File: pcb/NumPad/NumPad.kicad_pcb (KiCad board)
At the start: 2 copper layers, 100 x 100 mm, 120 parts, among them IC1 IS31FL3731, J1 USB_OTG, J2 ISP, J3 GS2, J4 GS2, J5 GS2, J6 GS2, J7 Conn_01x06, SW1 +, SW10 ,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

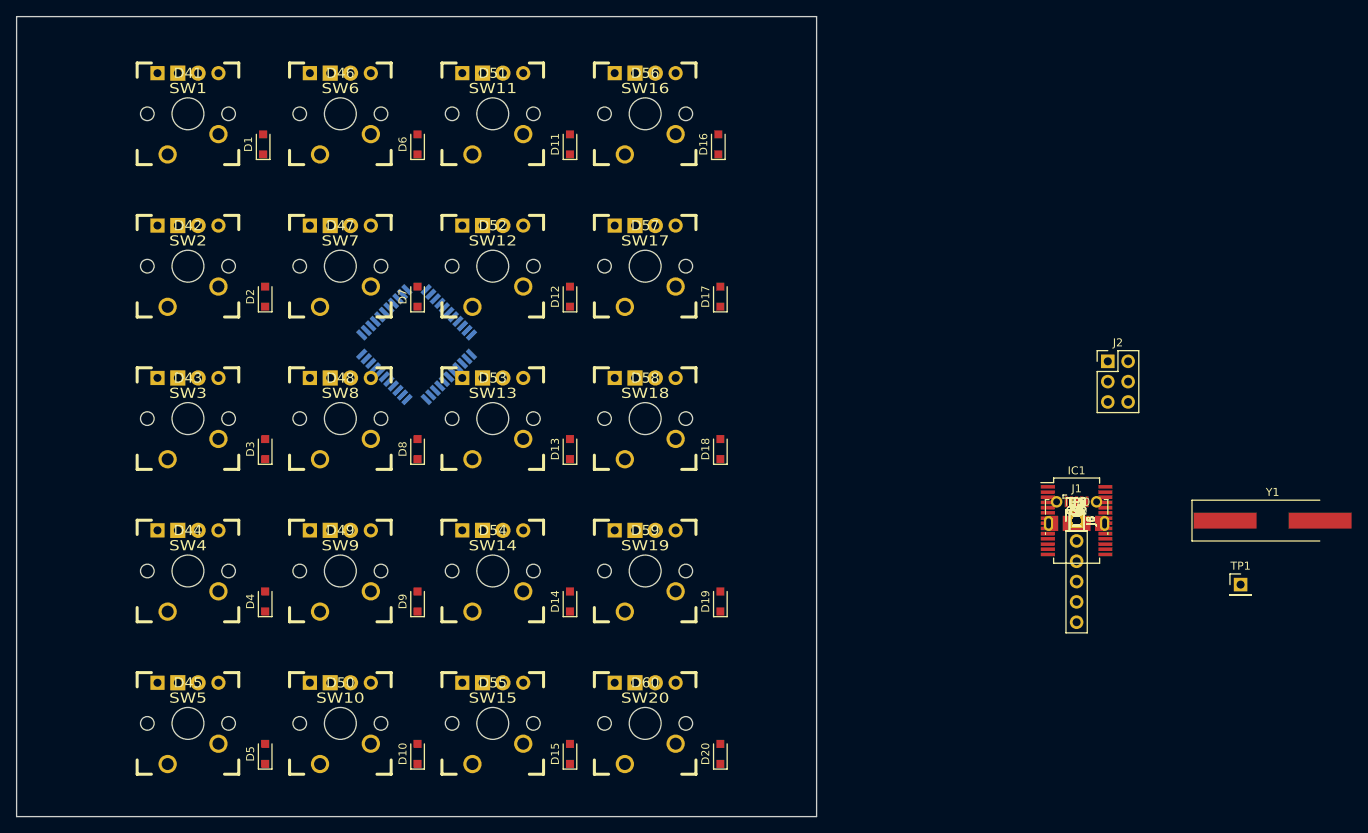
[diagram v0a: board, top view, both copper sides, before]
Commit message: changes in Numpad
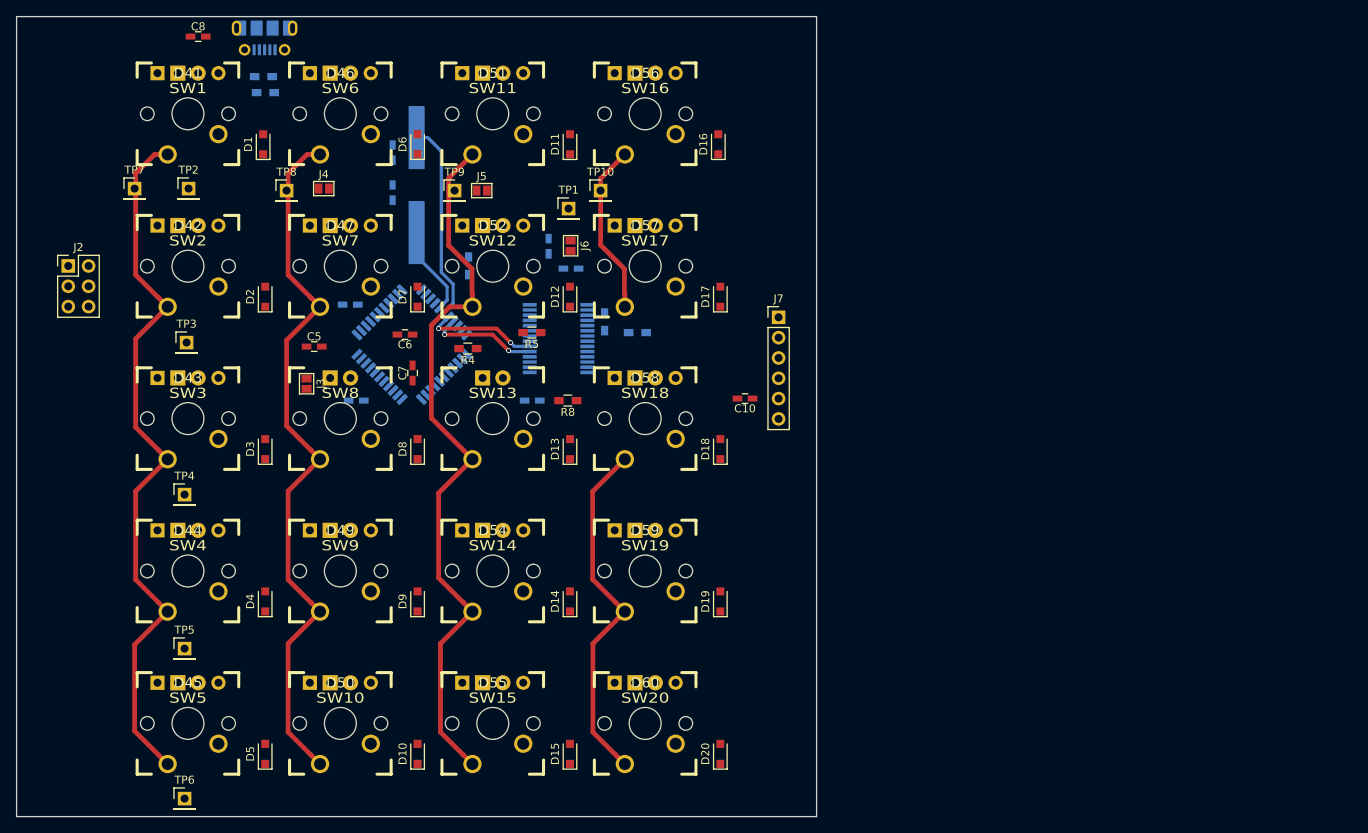
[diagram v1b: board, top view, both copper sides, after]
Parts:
- removed D48, D53: D, footprints:CHERRY_MX_DIODE
- C1, C11, C12, C2, C3, C4, C9, IC1, J1, R1, R2, R3, R6, R7, Y1: moved to B.Cu
- moved J2 130.5 mm to (47.5, 72.2)
- moved C8 125.4 mm to (63.7, 43.5)
- moved TP7 124.9 mm to (55.8, 62.5)
- moved J1 118.5 mm to (72.0, 42.8)
- moved TP2 118.5 mm to (62.5, 62.5)
- moved TP6 116.8 mm to (62.0, 138.8)
- moved R1 115.8 mm to (71.8, 48.5)
- moved Y1 114.9 mm to (91.0, 62.1), turned to 270 degrees
- moved R2 114.7 mm to (72.1, 50.5)
- moved TP3 113.5 mm to (62.2, 81.8)
- moved TP5 112.6 mm to (62.0, 120.0)
- moved TP4 111.5 mm to (62.0, 100.8)
- moved TP8 107.0 mm to (74.8, 62.8)
- moved J4 102.9 mm to (79.4, 62.5), turned to 90 degrees
- moved J3 97.8 mm to (77.2, 86.9)
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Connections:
- TP1 pad 1: Net-(TP1-Pad1) -> /Controller/SHUTDOWN
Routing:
- net /Controller/COL2: track 0.00 -> 91.4 mm
- net /Controller/COL1: track 0.00 -> 90.5 mm
- net /Controller/COL0: track 0.00 -> 90.5 mm
- net /Controller/COL3: track 0.00 -> 66.3 mm
- net Net-(C3-Pad1): track 0.00 -> 25.0 mm
- net /Controller/SCL: track 0.00 -> 14.3 mm, vias 0 -> 2
- net /Controller/SDA: track 0.00 -> 13.6 mm, vias 0 -> 2
- net Net-(C4-Pad1): track 0.00 -> 11.4 mm
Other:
- net class Default: clearance 0.2 -> 0.3
- rule trace_clearance: 0.2 -> 0.3

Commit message: changes in NumPad layout
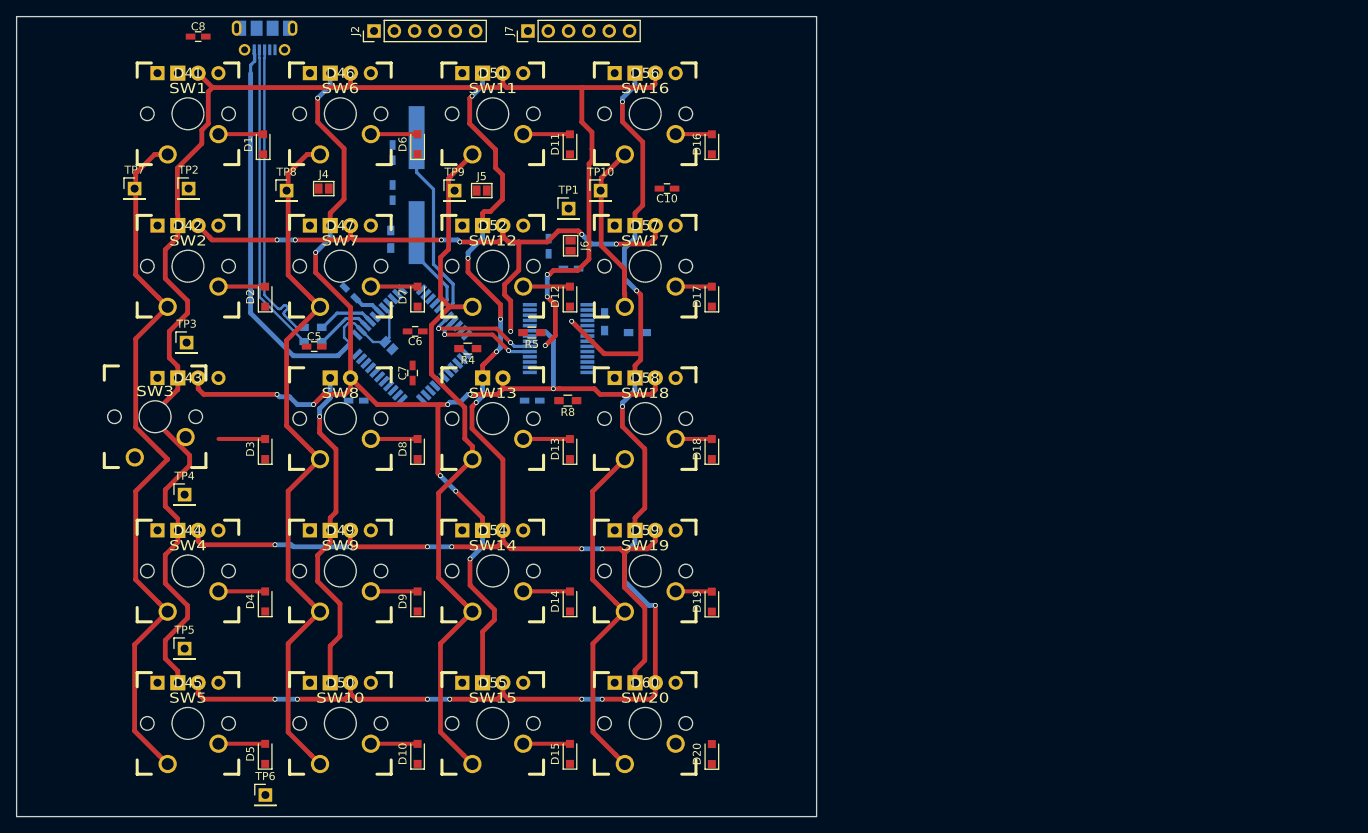
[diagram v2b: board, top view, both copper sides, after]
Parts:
- J2: footprint Pin_Headers:Pin_Header_Straight_2x03_Pitch2.54mm -> Pin_Headers:Pin_Header_Straight_1x06_Pitch2.54mm
- J3: moved to B.Cu
- moved J2 48.2 mm to (85.7, 42.8), turned to 90 degrees
- moved J7 47.6 mm to (104.9, 42.8), turned to 90 degrees
- moved R1 31.9 mm to (78.0, 79.8), turned to 180 degrees
- moved R2 31.7 mm to (78.0, 81.6), turned to 180 degrees
- moved C10 28.0 mm to (122.3, 62.5)
- moved J3 11.3 mm to (87.5, 82.1), turned to 45 degrees
- moved R3 10.3 mm to (87.8, 68.8), turned to 90 degrees
- moved TP6 10.1 mm to (72.1, 138.3)
- moved SW3 4.11 mm to (58.3, 91.0)
- moved C2 1.48 mm to (82.7, 75.5), turned to 315 degrees
- moved C6 1.34 mm to (90.8, 80.3)
- moved D19 1.06 mm to (127.9, 114.1)
- moved D20 1.06 mm to (127.9, 133.2)
- moved D17 1.06 mm to (127.9, 76.0)
- moved D18 1.06 mm to (127.9, 95.1)
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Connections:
- net Net-(J1-Pad2) renamed /Controller/USB_D-
- net Net-(J1-Pad3) renamed /Controller/USB_D+
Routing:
- net /Controller/CA1: track 0.00 -> 187.9 mm, vias 0 -> 3
- net /Controller/CA5: track 0.00 -> 159.6 mm, vias 0 -> 11
- net /Controller/CA3: track 0.00 -> 157.7 mm, vias 0 -> 10
- net /Controller/CA4: track 0.00 -> 149.4 mm, vias 0 -> 11
- net /Controller/CA2: track 0.00 -> 120.6 mm, vias 0 -> 8
- net UVCC: track 0.00 -> 61.9 mm
- net /Controller/USB_D-: track 0.00 -> 38.8 mm
- net /Controller/USB_D+: track 0.00 -> 38.8 mm
- net /Controller/D-: track 0.00 -> 7.41 mm
- net /Controller/D+: track 0.00 -> 7.28 mm
- net Net-(D7-Pad2): track 0.00 -> 5.85 mm
- net Net-(D5-Pad2): track 0.00 -> 5.85 mm
- net Net-(D2-Pad2): track 0.00 -> 5.85 mm
- net Net-(D15-Pad2): track 0.00 -> 5.85 mm
- net Net-(D12-Pad2): track 0.00 -> 5.85 mm
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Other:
- net class Default: clearance 0.3 -> 0.25; trace_width 0.25 -> 0.2
- net class IL_LEDS added: clearance 0.3, trace_width 0.6, via_dia 0.6, via_drill 0.4
- net class SWITCHES added: clearance 0.3, trace_width 0.6, via_dia 0.6, via_drill 0.4
- rule trace_clearance: 0.3 -> 0.25
- rule trace_min: 0.2 -> 0.1

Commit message: NumPad row and col routed
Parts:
- C1: moved to F.Cu
- moved TP4 65.4 mm to (127.4, 99.9)
- moved TP5 65.2 mm to (127.1, 119.2)
- moved TP3 64.9 mm to (127.1, 82.1)
- moved TP2 64.7 mm to (127.1, 61.3)
- moved TP6 38.1 mm to (110.1, 137.0)
- moved R3 26.9 mm to (100.2, 45.0), turned to 0 degrees
- moved C10 18.6 mm to (116.0, 45.0), turned to 0 degrees
- moved R5 10.3 mm to (95.5, 83.4)
- moved J6 9.77 mm to (117.0, 62.6), turned to 90 degrees
- moved C1 7.49 mm to (87.8, 82.9), turned to 180 degrees
- moved J3 7.03 mm to (80.7, 83.7), turned to 90 degrees
- moved SW3 4.11 mm to (62.4, 91.2)
- moved J4 0.95 mm to (78.5, 62.8)
- moved R4 0.74 mm to (97.0, 81.9), turned to 0 degrees
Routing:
- net /Controller/ROW1: track 0.00 -> 124.6 mm, vias 0 -> 7
- net /Controller/ROW0: track 0.00 -> 112.1 mm, vias 0 -> 13
- net /Controller/ROW3: track 0.00 -> 97.0 mm, vias 0 -> 7
- net /Controller/ROW2: track 0.00 -> 87.8 mm, vias 0 -> 7
- net /Controller/MISO: track 0.00 -> 77.8 mm, vias 0 -> 6
- net /Controller/ROW4: track 0.00 -> 64.4 mm
- net /Controller/COL0: track 90.5 -> 134.7 mm, vias 0 -> 4
- net /Controller/MOSI: track 0.00 -> 44.2 mm, vias 0 -> 3
- net /Controller/SCK: track 0.00 -> 43.2 mm, vias 0 -> 1
- net VCC: track 0.00 -> 39.1 mm, vias 0 -> 3
- net /Controller/COL2: track 91.1 -> 97.2 mm
- net Net-(C1-Pad2): track 0.00 -> 4.88 mm, vias 0 -> 1
- net Net-(D20-Pad2): track 0.00 -> 4.55 mm
- net /Controller/COL3: track 66.2 -> 70.3 mm
- net /Controller/SCL: track 14.3 -> 18.0 mm
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- added copper zone on B.Cu, net GND
- added copper zone on F.Cu, net GND
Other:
- net class Default: clearance 0.25 -> 0.2
- rule trace_clearance: 0.25 -> 0.2
